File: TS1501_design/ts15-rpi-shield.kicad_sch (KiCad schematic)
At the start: 14 parts, among them CON1 TROPIC01, IC1 TROPIC01_chip, J1 RPI socket, J2 CS select jumper switch

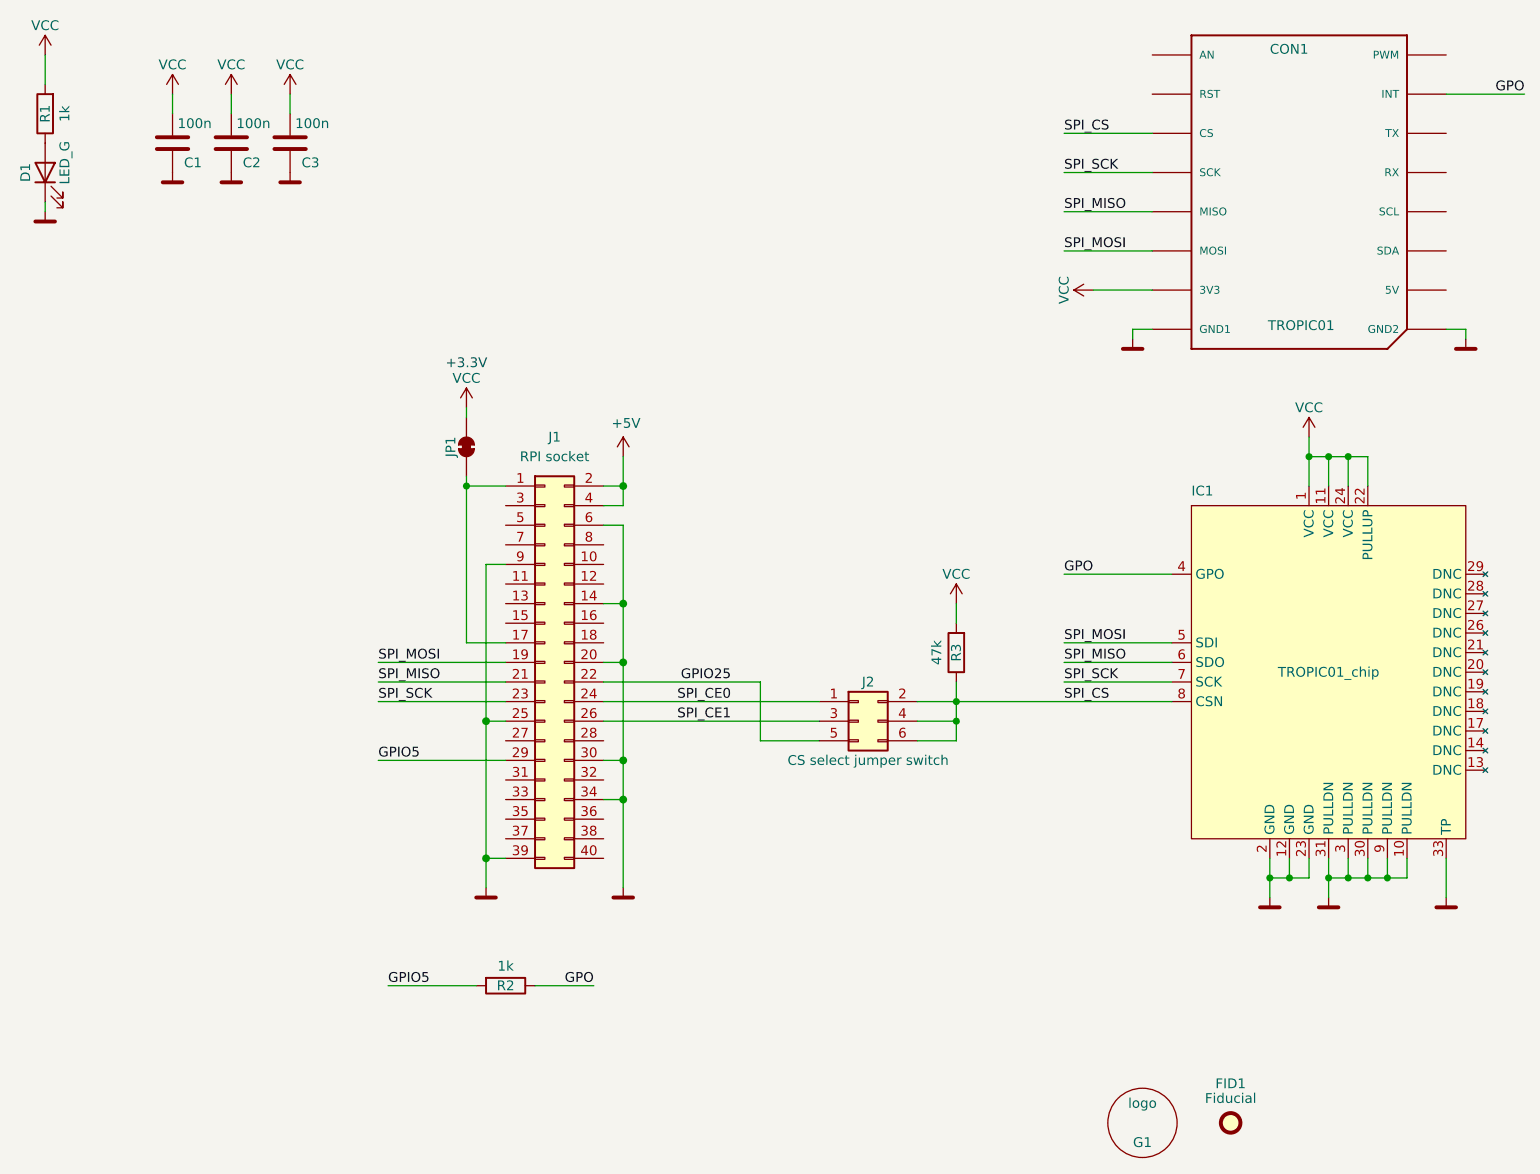
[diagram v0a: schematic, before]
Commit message: fix: Update BOM to fix wrong assembly of MIKROE socket
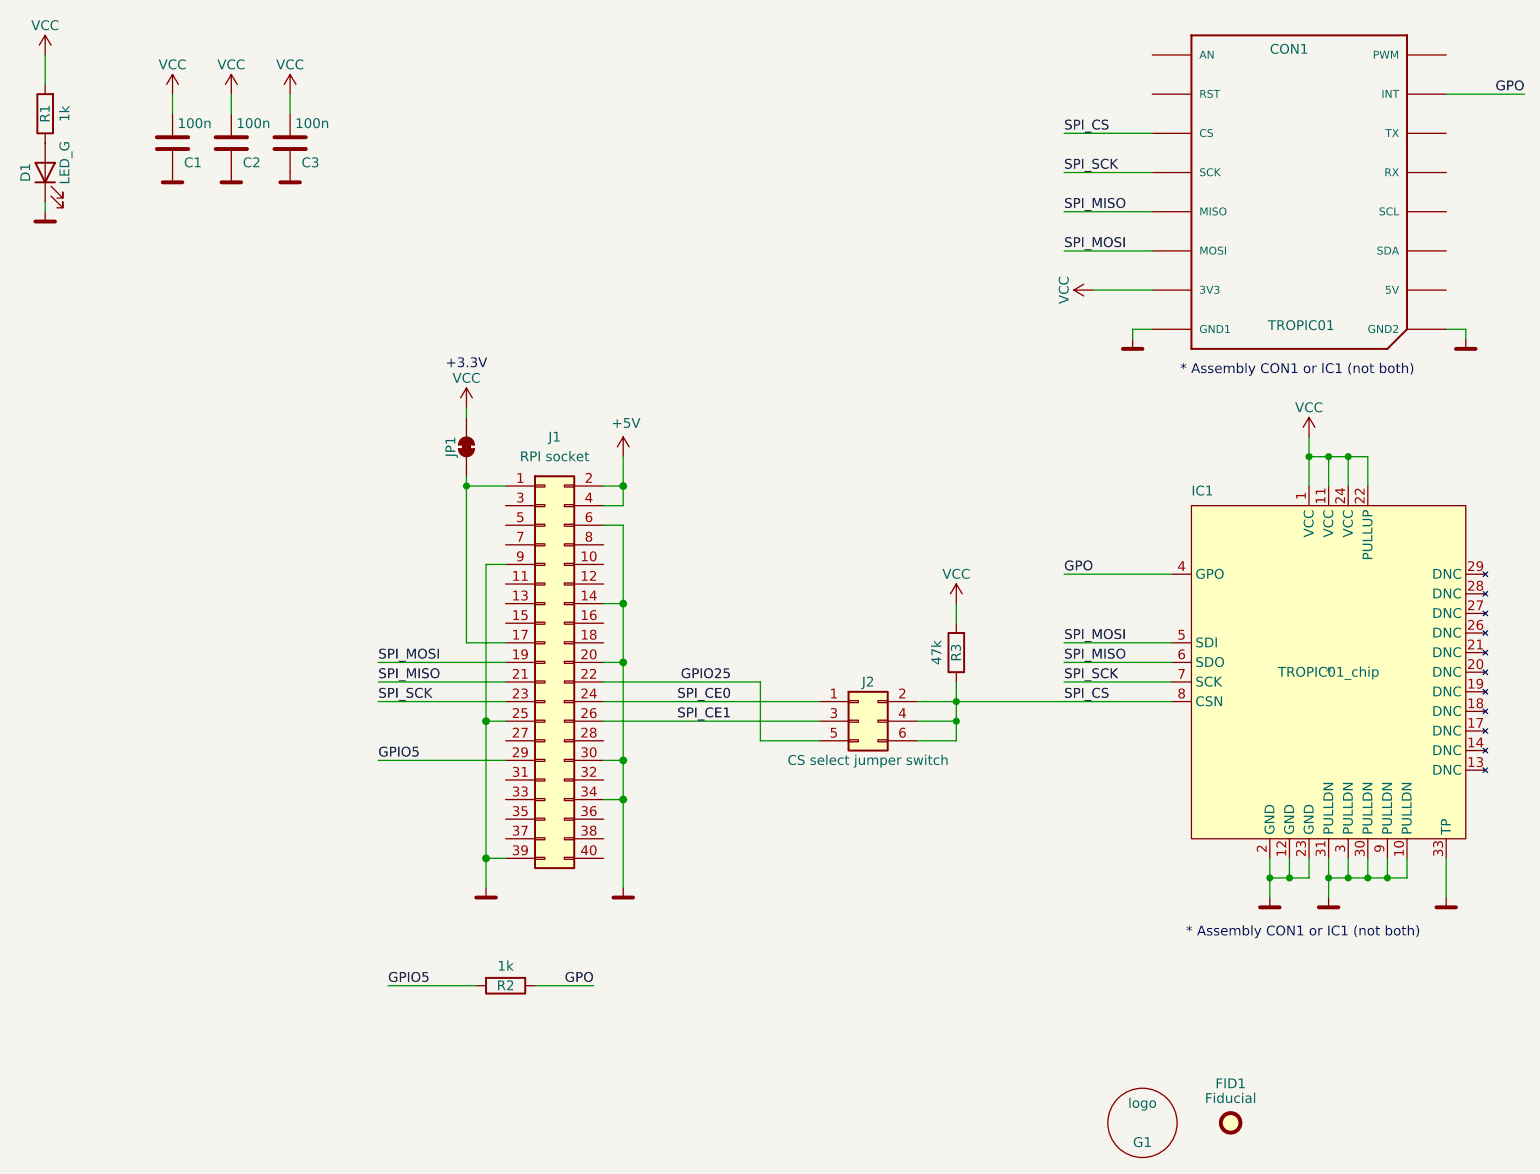
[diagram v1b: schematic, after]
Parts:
- CON1: OC_MOUSER 932-MIKROE-4247 -> * 932-MIKROE-4247
- IC1: OC_MOUSER (none) -> *
- J1: OC_MOUSER 474-PRT-16763 -> 474-PRT-16764
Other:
- note added: "* Assembly CON1 or IC1 (not both)"
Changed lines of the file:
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@@
 (kicad_sch
-	(version 20231120)
+	(version 20250114)
 	(generator "eeschema")
-	(generator_version "8.0")
+	(generator_version "9.0")
 	(paper "A4")
 	(title_block
@@
 		(rev "TS1501")
 	)
+	(text "+3.3V"
+		(exclude_from_sim no)
+		(at 99.06 75.692 0)
+		(effects
+			(font
+				(size 1.27 1.27)
+			)
+		)
+	)
+	(text "* Assembly CON1 or IC1 (not both)"
+		(exclude_from_sim no)
+		(at 206.756 76.454 0)
+		(effects
+			(font
+				(size 1.27 1.27)
+			)
+		)
+	)
+	(text "* Assembly CON1 or IC1 (not both)"
+		(exclude_from_sim no)
+		(at 207.518 149.352 0)
+		(effects
+			(font
+				(size 1.27 1.27)
+			)
+		)
+	)
 	(junction
 		(at 119.38 127)
@@
 		)
 	)
-	(text "+3.3V"
-		(exclude_from_sim no)
-		(at 99.06 75.692 0)
-		(effects
-			(font
-				(size 1.27 1.27)
-			)
-		)
-	)
 	(label "GPO"
 		(at 176.53 102.87 0)
-		(fields_autoplaced yes)
 		(effects
 			(font
@@
 	(label "GPIO25"
 		(at 133.35 116.84 180)
-		(fields_autoplaced yes)
 		(effects
 			(font
@@
 	(label "SPI_CE0"
 		(at 133.35 119.38 180)
-		(fields_autoplaced yes)
 		(effects
 			(font
@@
 	(label "GPIO5"
 		(at 87.63 127 0)
-		(fields_autoplaced yes)
 		(effects
 			(font
@@
 	(label "SPI_MISO"
 		(at 87.63 116.84 0)
-		(fields_autoplaced yes)
 		(effects
 			(font
@@
 	(label "GPIO5"
 		(at 88.9 156.21 0)
-		(fields_autoplaced yes)
 		(effects
 			(font
@@
 	(label "SPI_MOSI"
 		(at 176.53 111.76 0)
-		(fields_autoplaced yes)
 		(effects
 			(font
@@
 	(label "SPI_CS"
 		(at 176.53 119.38 0)
-		(fields_autoplaced yes)
 		(effects
 			(font
@@
 	(label "SPI_MOSI"
 		(at 176.53 60.96 0)
-		(fields_autoplaced yes)
 		(effects
 			(font
@@
 	(label "SPI_MISO"
 		(at 176.53 55.88 0)
-		(fields_autoplaced yes)
 		(effects
 			(font
@@
 	(label "SPI_SCK"
 		(at 87.63 119.38 0)
-		(fields_autoplaced yes)
 		(effects
 			(font
@@
 	(label "SPI_CS"
 		(at 176.53 45.72 0)
-		(fields_autoplaced yes)
 		(effects
 			(font
@@
 	(label "SPI_MISO"
 		(at 176.53 114.3 0)
-		(fields_autoplaced yes)
 		(effects
 			(font
@@
 	(label "SPI_SCK"
 		(at 176.53 116.84 0)
-		(fields_autoplaced yes)
 		(effects
 			(font
@@
 	(label "GPO"
 		(at 236.22 40.64 180)
-		(fields_autoplaced yes)
 		(effects
 			(font
@@
 	(label "SPI_MOSI"
 		(at 87.63 114.3 0)
-		(fields_autoplaced yes)
 		(effects
 			(font
@@
 	(label "GPO"
 		(at 115.57 156.21 180)
-		(fields_autoplaced yes)
 		(effects
 			(font
@@
 	(label "SPI_CE1"
 		(at 133.35 121.92 180)
-		(fields_autoplaced yes)
 		(effects
 			(font
@@
 	(label "SPI_SCK"
 		(at 176.53 50.8 0)
-		(fields_autoplaced yes)
 		(effects
 			(font
@@
 			)
 		)
+		(property "Sim.Device" ""
+			(at 60.96 46.99 0)
+			(effects
+				(font
+					(size 1.27 1.27)
+				)
+			)
+		)
 		(pin "1"
 		)
@@
 			)
 		)
+		(property "OC_MOUSER" "*"
+			(at 210.82 115.57 0)
+			(effects
+				(font
+					(size 1.27 1.27)
+				)
+			)
+		)
+		(property "Sim.Device" ""
+			(at 210.82 115.57 0)
+			(effects
+				(font
+					(size 1.27 1.27)
+				)
+			)
+		)
 		(pin "7"
 		)
@@
 			)
 		)
-		(property "OC_MOUSER" "474-PRT-16763"
+		(property "OC_MOUSER" "474-PRT-16764"
 			(at 109.22 114.3 0)
 			(effects
@@
 					(size 1.27 1.27)
 				)
-				(hide yes)
 			)
 		)
@@
 			)
 		)
+		(property "Sim.Device" ""
+			(at 149.86 121.92 0)
+			(effects
+				(font
+					(size 1.27 1.27)
+				)
+			)
+		)
 		(pin "4"
 		)
@@
 			)
 		)
+		(property "Sim.Device" ""
+			(at 162.56 113.03 0)
+			(effects
+				(font
+					(size 1.27 1.27)
+				)
+			)
+		)
 		(pin "1"
 		)
@@
 			)
 		)
+		(property "Sim.Device" ""
+			(at 186.69 173.99 0)
+			(effects
+				(font
+					(size 1.27 1.27)
+				)
+			)
+		)
 		(instances
 			(project ""
@@
 			)
 		)
+		(property "Sim.Device" ""
+			(at 44.45 43.18 0)
+			(effects
+				(font
+					(size 1.27 1.27)
+				)
+			)
+		)
 		(pin "1"
 		)
@@
 			)
 		)
+		(property "Sim.Device" ""
+			(at 68.58 46.99 0)
+			(effects
+				(font
+					(size 1.27 1.27)
+				)
+			)
+		)
 		(pin "1"
 		)
@@
 			)
 		)
+		(property "Sim.Device" ""
+			(at 198.12 173.99 0)
+			(effects
+				(font
+					(size 1.27 1.27)
+				)
+			)
+		)
 		(instances
 			(project "ts14-arduino-shield"
@@
 			)
 		)
+		(property "Sim.Device" ""
+			(at 76.2 46.99 0)
+			(effects
+				(font
+					(size 1.27 1.27)
+				)
+			)
+		)
 		(pin "1"
 		)
@@
 			)
 		)
+		(property "Sim.Device" ""
+			(at 99.06 86.36 0)
+			(effects
+				(font
+					(size 1.27 1.27)
+				)
+			)
+		)
 		(pin "2"
 		)
@@
 			)
 		)
+		(property "Sim.Device" ""
+			(at 44.45 50.8 0)
+			(effects
+				(font
+					(size 1.27 1.27)
+				)
+			)
+		)
 		(pin "1"
 		)
@@
 			)
 		)
+		(property "Sim.Device" ""
+			(at 104.14 156.21 0)
+			(effects
+				(font
+					(size 1.27 1.27)
+				)
+			)
+		)
 		(pin "1"
 		)
@@
 			)
 		)
-		(property "OC_MOUSER" "932-MIKROE-4247"
+		(property "OC_MOUSER" "* 932-MIKROE-4247"
 			(at 193.04 73.66 0)
 			(effects
@@
 			)
 		)
+		(property "Sim.Device" ""
+			(at 193.04 73.66 0)
+			(effects
+				(font
+					(size 1.27 1.27)
+				)
+			)
+		)
 		(pin "P8"
 		)
@@
 		)
 	)
+	(embedded_fonts no)
 )
